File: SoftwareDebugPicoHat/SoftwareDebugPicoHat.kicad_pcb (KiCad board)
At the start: 4 copper layers, 69 x 54.7 mm, 14 parts, among them J1 35362-0950, J2 Conn_Coaxial, J3 USB_C_Receptacle_USB2.0_14P, J4 Conn_Coaxial, J5 Conn_01x04_Pin, U1 RFM98PW, U3 LORA1280F27-TCXO

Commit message: Updated to throughhole pico
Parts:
- A1: footprint Module:RaspberryPi_Pico_SMD_HandSolder -> Module:RaspberryPi_Pico_Common_THT
- moved A1 26.0 mm to (151.5, 55.3)
- moved C2 0.11 mm to (132.0, 105.2)
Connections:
- C3 pad 1: +3V3 -> +5V
- D1 pad 1: +3V3 -> +5V
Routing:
- net +5V: track 127.7 -> 147.0 mm, vias 7 -> 8
- net +3V3: track 132.6 -> 117.2 mm
- net UHF_MISO: track 9.49 -> 11.1 mm
- net UHF_SCLK: track 16.5 -> 18.1 mm
- net UHF_RST: track 22.1 -> 23.7 mm
- net UHF_D0: track 12.4 -> 14.0 mm
- net UHF_CS: track 17.1 -> 18.7 mm
- net UHF_MOSI: track 15.5 -> 17.1 mm, vias 2 -> 1
- net SBAND_D1: track 39.7 -> 38.1 mm, vias 2 -> 1
- net NEOPIXEL: track 23.3 -> 24.8 mm, vias 2 -> 1
- net GND: track 19.6 -> 21.0 mm, vias 122 -> 131
- net SBAND_RST: track 29.7 -> 30.8 mm, vias 4 -> 3
- net SBAND_RXEN: vias 2 -> 1
- net SBAND_CS: track 13.1 -> 13.2 mm, vias 2 -> 1
- net SBAND_BUSY: vias 4 -> 3
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
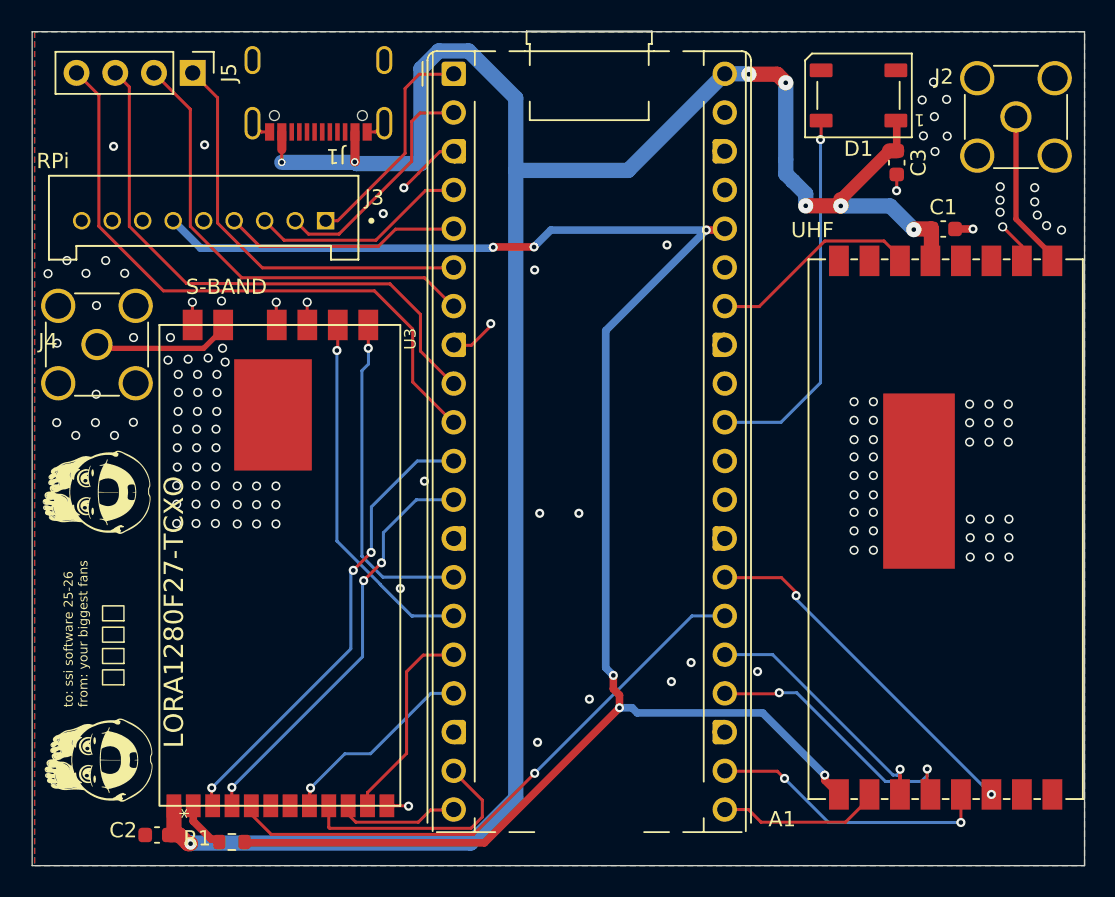
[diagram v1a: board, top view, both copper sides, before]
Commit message: RELEASE: 1 ) Updated some component locations for better placement
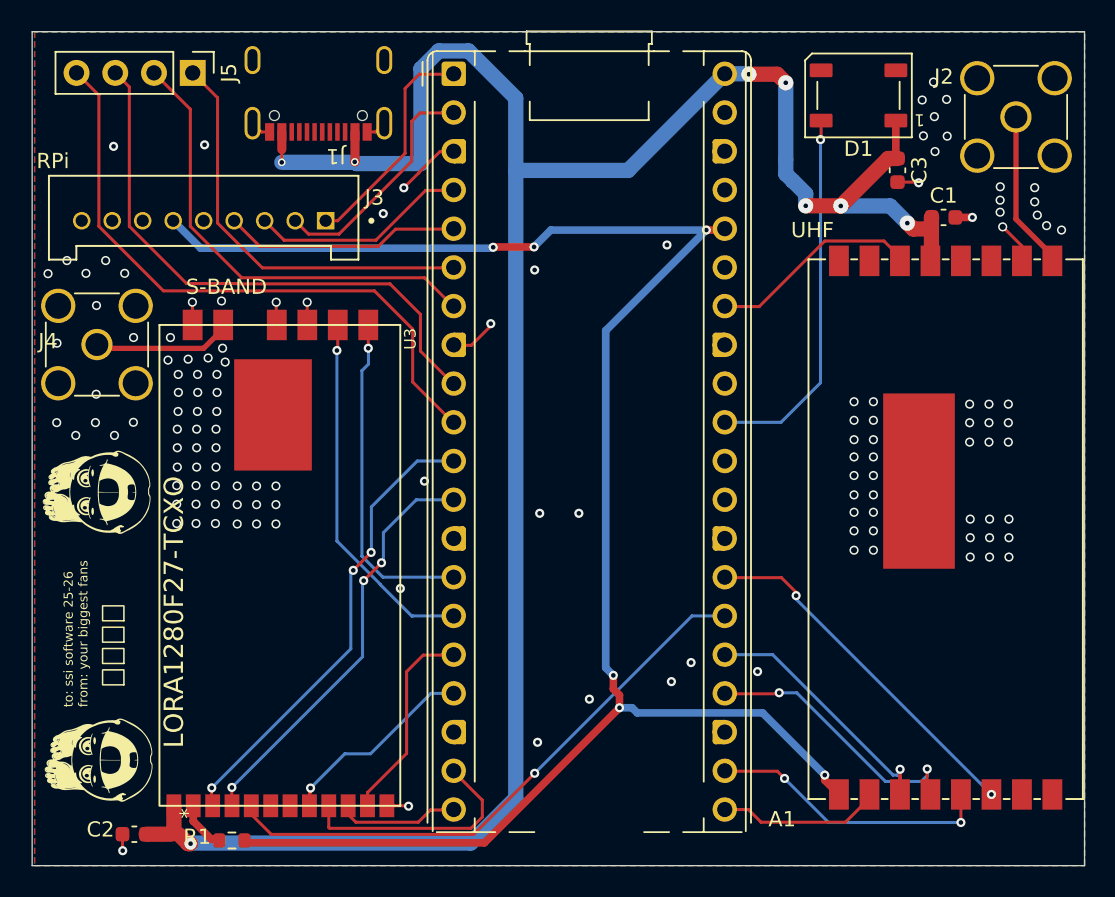
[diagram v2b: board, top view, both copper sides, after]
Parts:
- moved C2 1.49 mm to (130.5, 105.2)
- moved C1 0.76 mm to (183.6, 64.7)
- moved C3 0.50 mm to (180.6, 61.6)
- moved R1 0.10 mm to (136.9, 105.6)
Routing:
- net +5V: track 147.0 -> 149.4 mm
- net GND: track 21.0 -> 22.4 mm, vias 131 -> 132
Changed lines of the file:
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@@
 	(footprint "Resistor_SMD:R_0603_1608Metric"
 		(layer "F.Cu")
-		(at 136.92 105.71 180)
+		(at 136.92 105.61 180)
 		(descr "Resistor SMD 0603 (1608 Metric), square (rectangular) end terminal, IPC-7351 nominal, (Body size source: IPC-SM-782 page 72, https://www.pcb-3d.com/wordpress/wp-content/uploads/ipc-sm-782a_amendment_1_and_2.pdf), generated with kicad-footprint-generator")
 		(tags "resistor")
@@
 	(footprint "Capacitor_SMD:C_0603_1608Metric"
 		(layer "F.Cu")
-		(at 180.53 61.15 -90)
+		(at 180.58 61.65 -90)
 		(descr "Capacitor SMD 0603 (1608 Metric), square (rectangular) end terminal, IPC-7351 nominal, (Body size source: IPC-SM-782 page 76, https://www.pcb-3d.com/wordpress/wp-content/uploads/ipc-sm-782a_amendment_1_and_2.pdf), generated with kicad-footprint-generator")
 		(tags "capacitor")
@@
 	(footprint "Capacitor_SMD:C_0603_1608Metric"
 		(layer "F.Cu")
-		(at 132.01 105.25 180)
+		(at 130.52 105.2 180)
 		(descr "Capacitor SMD 0603 (1608 Metric), square (rectangular) end terminal, IPC-7351 nominal, (Body size source: IPC-SM-782 page 76, https://www.pcb-3d.com/wordpress/wp-content/uploads/ipc-sm-782a_amendment_1_and_2.pdf), generated with kicad-footprint-generator")
 		(tags "capacitor")
@@
 	(footprint "Capacitor_SMD:C_0603_1608Metric"
 		(layer "F.Cu")
-		(at 183.58 65.5)
+		(at 183.6 64.74)
 		(descr "Capacitor SMD 0603 (1608 Metric), square (rectangular) end terminal, IPC-7351 nominal, (Body size source: IPC-SM-782 page 76, https://www.pcb-3d.com/wordpress/wp-content/uploads/ipc-sm-782a_amendment_1_and_2.pdf), generated with kicad-footprint-generator")
 		(tags "capacitor")
@@
 	)
 	(segment
+		(start 181.925 62.425)
+		(end 180.58 62.425)
+		(width 0.2)
+		(layer "F.Cu")
+		(net 7)
+	)
+	(segment
 		(start 134.33 70.3)
 		(end 134.33 71.77825)
@@
 	)
 	(segment
-		(start 139.395 59.135)
-		(end 138.85 59.135)
+		(start 129.745 106.265)
+		(end 129.76 106.28)
 		(width 0.2)
 		(layer "F.Cu")
@@
 	)
 	(segment
-		(start 148.51 103.36)
-		(end 148.485 103.335)
+		(start 129.745 105.2)
+		(end 129.745 106.265)
+		(width 0.2)
+		(layer "F.Cu")
+		(net 7)
+	)
+	(segment
+		(start 139.395 59.135)
+		(end 138.85 59.135)
 		(width 0.2)
 		(layer "F.Cu")
@@
 	)
 	(segment
-		(start 180.53 62.98)
-		(end 180.52 62.99)
+		(start 148.51 103.36)
+		(end 148.485 103.335)
 		(width 0.2)
 		(layer "F.Cu")
@@
 	)
 	(segment
-		(start 184.355 65.5)
-		(end 185.53 65.5)
-		(width 0.5)
+		(start 153.9 71.71)
+		(end 153.9 71.86)
+		(width 0.2)
 		(layer "F.Cu")
 		(net 7)
 	)
 	(segment
-		(start 180.53 61.925)
-		(end 180.53 62.98)
+		(start 141.86 70.301)
+		(end 141.86 71.78825)
 		(width 0.2)
 		(layer "F.Cu")
@@
 	)
 	(segment
-		(start 153.9 71.71)
-		(end 153.9 71.86)
+		(start 139.83 71.75825)
+		(end 139.86675 71.795)
 		(width 0.2)
 		(layer "F.Cu")
@@
 	)
 	(segment
-		(start 141.86 70.301)
-		(end 141.86 71.78825)
+		(start 181.97 62.47)
+		(end 181.925 62.425)
 		(width 0.2)
 		(layer "F.Cu")
@@
 	)
 	(segment
-		(start 139.83 71.75825)
-		(end 139.86675 71.795)
-		(width 0.2)
+		(start 184.375 64.74)
+		(end 185.49 64.74)
+		(width 0.5)
 		(layer "F.Cu")
 		(net 7)
@@
 	)
 	(via
+		(at 129.76 106.28)
+		(size 0.6)
+		(drill 0.3)
+		(layers "F.Cu" "B.Cu")
+		(free yes)
+		(net 7)
+	)
+	(via
 		(at 133.34 81.12)
 		(size 0.6)
@@
 	)
 	(via
-		(at 185.53 65.5)
+		(at 185.49 64.74)
 		(size 0.6)
 		(drill 0.3)
@@
 	)
 	(via
-		(at 180.52 62.99)
+		(at 181.97 62.47)
 		(size 0.6)
 		(drill 0.3)
@@
 	)
 	(segment
-		(start 134.21 105.82)
-		(end 134.05 105.82)
+		(start 181.225 65.115)
+		(end 181.61 65.5)
 		(width 1)
 		(layer "F.Cu")
@@
 	)
 	(segment
-		(start 182.805 65.5)
-		(end 182.805 67.525)
+		(start 134.21 105.82)
+		(end 134.05 105.82)
 		(width 1)
 		(layer "F.Cu")
@@
 	)
 	(segment
-		(start 180.055 60.375)
-		(end 180.53 60.375)
+		(start 182.805 65.5)
+		(end 182.805 67.525)
 		(width 1)
 		(layer "F.Cu")
@@
 	)
 	(segment
+		(start 180.47 58.39)
+		(end 180.47 60.765)
+		(width 0.5)
+		(layer "F.Cu")
+		(net 13)
+	)
+	(segment
 		(start 172.69 55.35)
 		(end 173.25 55.91)
@@
 	)
 	(segment
+		(start 132.935 105.2)
+		(end 133.11675 105.01825)
+		(width 0.2)
+		(layer "F.Cu")
+		(net 13)
+	)
+	(segment
 		(start 140.195 60.295)
 		(end 140.19 60.3)
@@
 	)
 	(segment
+		(start 131.295 105.2)
+		(end 132.935 105.2)
+		(width 1)
+		(layer "F.Cu")
+		(net 13)
+	)
+	(segment
 		(start 133.11675 103.335)
 		(end 133.11675 105.01825)
@@
 	)
 	(segment
-		(start 180.53 60.375)
-		(end 180.53 58.45)
-		(width 0.5)
+		(start 181.305 65.115)
+		(end 181.225 65.115)
+		(width 0.2)
 		(layer "F.Cu")
 		(net 13)
 	)
 	(segment
-		(start 140.19 60.3)
-		(end 140.19 61.13)
-		(width 0.2)
+		(start 180.47 60.765)
+		(end 180.58 60.875)
+		(width 0.5)
 		(layer "F.Cu")
 		(net 13)
 	)
 	(segment
-		(start 182.805 67.525)
-		(end 182.74 67.59)
+		(start 140.19 60.3)
+		(end 140.19 61.13)
 		(width 0.2)
 		(layer "F.Cu")
@@
 	(segment
 		(start 182.805 65.5)
-		(end 181.69 65.5)
+		(end 182.805 64.76)
 		(width 1)
 		(layer "F.Cu")
@@
 	)
 	(segment
-		(start 140.195 59.135)
-		(end 140.195 60.295)
-		(width 0.6)
+		(start 179.975 60.875)
+		(end 180.58 60.875)
+		(width 1)
 		(layer "F.Cu")
 		(net 13)
 	)
 	(segment
-		(start 176.86 63.57)
-		(end 180.055 60.375)
-		(width 0.8)
+		(start 182.805 67.525)
+		(end 182.74 67.59)
+		(width 0.2)
 		(layer "F.Cu")
 		(net 13)
 	)
 	(segment
-		(start 181.69 65.5)
-		(end 181.65 65.54)
-		(width 0.2)
+		(start 182.805 64.76)
+		(end 182.825 64.74)
+		(width 1)
 		(layer "F.Cu")
 		(net 13)
 	)
 	(segment
-		(start 176.86 63.99)
-		(end 176.85 63.98)
-		(width 1)
+		(start 140.195 59.135)
+		(end 140.195 60.295)
+		(width 0.6)
 		(layer "F.Cu")
 		(net 13)
 	)
 	(segment
-		(start 133.47 105.24)
-		(end 132.895 105.24)
+		(start 176.86 63.99)
+		(end 179.975 60.875)
 		(width 1)
 		(layer "F.Cu")
@@
 	(segment
 		(start 176.86 63.99)
-		(end 176.86 63.57)
+		(end 176.85 63.98)
 		(width 1)
 		(layer "F.Cu")
@@
 	)
 	(segment
+		(start 181.61 65.5)
+		(end 182.805 65.5)
+		(width 1)
+		(layer "F.Cu")
+		(net 13)
+	)
+	(segment
 		(start 133.11675 105.01825)
 		(end 132.895 105.24)
@@
 	)
 	(via
-		(at 181.65 65.54)
+		(at 181.225 65.115)
 		(size 1)
 		(drill 0.3)
@@
 	)
 	(segment
+		(start 181.225 65.115)
+		(end 180.1 63.99)
+		(width 1)
+		(layer "B.Cu")
+		(net 13)
+	)
+	(segment
 		(start 144.98 61.1)
 		(end 144.95 61.13)
@@
 	)
 	(segment
-		(start 180.1 63.99)
-		(end 181.65 65.54)
-		(width 1)
-		(layer "B.Cu")
-		(net 13)
-	)
-	(segment
 		(start 149.32 54.990252)
 		(end 149.32 61.21)
@@
 	)
 	(segment
+		(start 180.1 63.99)
+		(end 176.86 63.99)
+		(width 1)
+		(layer "B.Cu")
+		(net 13)
+	)
+	(segment
 		(start 152.59 105.78)
 		(end 134.25 105.78)
@@
 	)
 	(segment
-		(start 176.86 63.99)
-		(end 180.1 63.99)
-		(width 1)
-		(layer "B.Cu")
-		(net 13)
-	)
-	(segment
 		(start 173.73 62.36)
 		(end 174.56 63.19)
@@
 	)
 	(segment
-		(start 153.487 105.763)
-		(end 137.798 105.763)
+		(start 175.81 101.66)
+		(end 176.74 102.59)
 		(width 0.5)
 		(layer "F.Cu")
@@
 	)
 	(segment
-		(start 162.345 96.905)
-		(end 153.487 105.763)
+		(start 137.745 105.61)
+		(end 137.745 105.71)
 		(width 0.5)
 		(layer "F.Cu")
@@
 	)
 	(segment
-		(start 175.81 101.66)
-		(end 176.74 102.59)
+		(start 169.16 65.57)
+		(end 169.25 65.48)
 		(width 0.5)
 		(layer "F.Cu")
@@
 	)
 	(segment
-		(start 137.798 105.763)
-		(end 137.745 105.71)
+		(start 162.345 96.905)
+		(end 153.487 105.763)
 		(width 0.5)
 		(layer "F.Cu")
@@
 	)
 	(segment
-		(start 169.16 65.57)
-		(end 169.25 65.48)
+		(start 137.898 105.763)
+		(end 137.745 105.61)
 		(width 0.5)
 		(layer "F.Cu")
@@
 	)
 	(segment
+		(start 153.487 105.763)
+		(end 137.898 105.763)
+		(width 0.5)
+		(layer "F.Cu")
+		(net 37)
+	)
+	(segment
 		(start 168.04 65.57)
 		(end 169.16 65.57)
@@
 	)
 	(segment
-		(start 134.38675 103.81175)
-		(end 134.38675 104.34675)
+		(start 135.57 105.53)
+		(end 136.105 105.53)
 		(width 0.5)
 		(layer "F.Cu")
@@
 	)
 	(segment
-		(start 134.38675 104.34675)
-		(end 135.57 105.53)
+		(start 134.38675 103.81175)
+		(end 134.38675 104.34675)
 		(width 0.5)
 		(layer "F.Cu")
@@
 	)
 	(segment
-		(start 135.57 105.53)
-		(end 136.105 105.53)
+		(start 134.38675 104.34675)
+		(end 135.57 105.53)
 		(width 0.5)
 		(layer "F.Cu")
